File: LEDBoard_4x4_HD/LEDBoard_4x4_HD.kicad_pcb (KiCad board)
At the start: 4 copper layers, 25 x 10 mm, 17 parts, among them U1 TLC5957

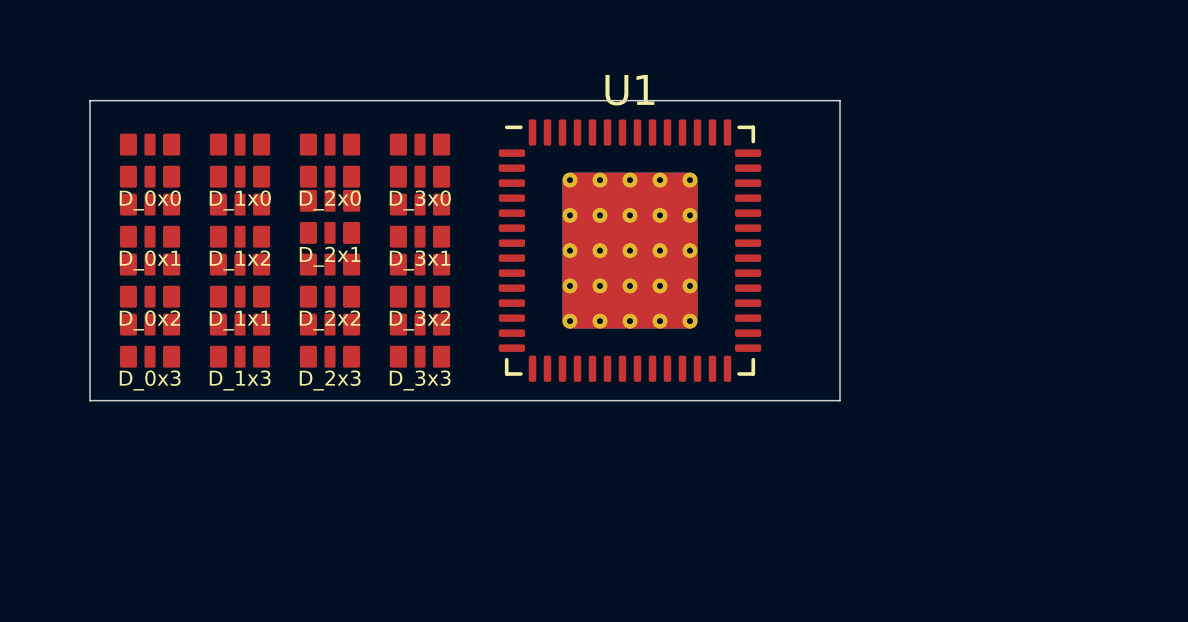
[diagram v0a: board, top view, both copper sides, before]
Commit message: LEDBoard parts positioned & routing started
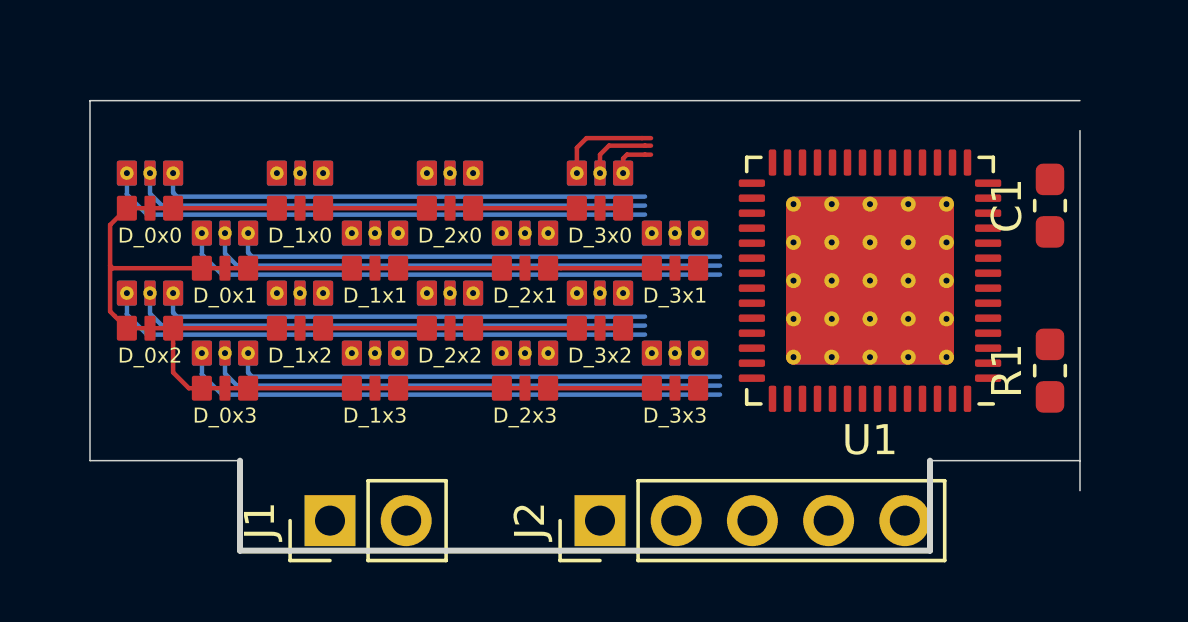
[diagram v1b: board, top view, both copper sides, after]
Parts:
- added C1: 0.1uF, Capacitor_SMD:C_0603_1608Metric_Pad1.05x0.95mm_HandSolder, F.Cu at (132.0, 103.5)
- added J1: power, Connector_PinHeader_2.54mm:PinHeader_1x02_P2.54mm_Vertical, F.Cu at (108.0, 114.0)
- added J2: data, Connector_PinHeader_2.54mm:PinHeader_1x05_P2.54mm_Vertical, F.Cu at (117.0, 114.0)
- added R1: 7.5KOhm 0.1%, Resistor_SMD:R_0603_1608Metric_Pad1.05x0.95mm_HandSolder, F.Cu at (132.0, 109.0)
- D_0x0, D_0x1, D_0x2, D_0x3, D_1x0, D_1x1, D_1x2, D_1x3, D_2x0, D_2x1, D_2x2, D_2x3, D_3x0, D_3x1, D_3x2, D_3x3: footprint LEDs_SMD_NICHIA:LED_RGB_0706_1816Metric_ROHM__VeryNarow -> LEDs_SMD_NICHIA:LED_RGB_0706_1816Metric_ROHM_ThermalVias
- U1: footprint Package_DFN_QFN:QFN-56-1EP_8x8mm_P0.5mm_EP4.5x5.2mm_ThermalVias -> Package_DFN_QFN:QFN-56-1EP_8x8mm_P0.5mm_EP5.6x5.6mm_ThermalVias
- moved D_3x1 8.56 mm to (119.5, 105.0)
- moved D_3x3 8.56 mm to (119.5, 109.0)
- moved U1 8.06 mm to (126.0, 106.0), turned to 180 degrees
- moved D_2x1 6.60 mm to (114.5, 105.0)
- moved D_2x3 6.58 mm to (114.5, 109.0)
- moved D_3x0 6.08 mm to (117.0, 103.0)
- moved D_3x2 6.08 mm to (117.0, 107.0)
- moved D_1x1 4.61 mm to (109.5, 105.0)
- moved D_1x3 4.61 mm to (109.5, 109.0)
- moved D_2x0 4.12 mm to (112.0, 103.0)
- moved D_2x2 4.12 mm to (112.0, 107.0)
- moved D_1x2 3.61 mm to (107.0, 107.0)
- moved D_0x1 2.69 mm to (104.5, 105.0)
- moved D_0x3 2.69 mm to (104.5, 109.0)
- moved D_1x0 2.24 mm to (107.0, 103.0)
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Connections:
- U1 pad 1: (no net) -> /IREF
- U1 pad 10: (no net) -> /led_0x0_b
- U1 pad 11: (no net) -> /led_1x0_r
- U1 pad 12: (no net) -> /led_1x0_g
- U1 pad 13: (no net) -> /led_1x0_b
- U1 pad 14: (no net) -> /led_2x0_r
- U1 pad 15: (no net) -> /led_2x0_g
- U1 pad 16: (no net) -> /led_2x0_b
- U1 pad 17: (no net) -> /led_3x0_r
- U1 pad 18: (no net) -> /led_3x0_g
- U1 pad 19: (no net) -> /led_3x0_b
- U1 pad 2: (no net) -> /led_2x3_r
- U1 pad 20: (no net) -> /led_0x1_r
- U1 pad 21: (no net) -> /led_0x1_g
- U1 pad 22: (no net) -> /led_0x1_b
- U1 pad 23: (no net) -> /led_1x1_r
- U1 pad 24: (no net) -> /led_1x1_g
- U1 pad 25: (no net) -> /led_1x1_b
- U1 pad 26: (no net) -> /SIN
- U1 pad 27: (no net) -> /LAT
- U1 pad 28: (no net) -> /SCLK
- U1 pad 29: (no net) -> /GCLK
- U1 pad 3: (no net) -> /led_2x3_g
- U1 pad 30: (no net) -> /led_2x1_r
- U1 pad 31: (no net) -> /led_2x1_g
- U1 pad 32: (no net) -> /led_2x1_b
- U1 pad 33: (no net) -> /led_3x1_r
- U1 pad 34: (no net) -> /led_3x1_g
- U1 pad 35: (no net) -> /led_3x1_b
- U1 pad 36: (no net) -> /led_0x2_r
- U1 pad 37: (no net) -> /led_0x2_g
- U1 pad 38: (no net) -> /led_0x2_b
- U1 pad 39: (no net) -> /led_1x2_r
- U1 pad 4: (no net) -> /led_2x3_b
- U1 pad 40: (no net) -> /led_1x2_g
- U1 pad 41: (no net) -> /led_1x2_b
- U1 pad 42: (no net) -> /SOUT
- U1 pad 43: (no net) -> VCC
- U1 pad 44: (no net) -> /led_2x2_r
- U1 pad 45: (no net) -> /led_2x2_g
- U1 pad 46: (no net) -> /led_2x2_b
- U1 pad 47: (no net) -> /led_3x2_r
- U1 pad 48: (no net) -> /led_3x2_g
- U1 pad 49: (no net) -> /led_3x2_b
- U1 pad 5: (no net) -> /led_3x3_r
- U1 pad 50: (no net) -> /led_0x3_r
- U1 pad 51: (no net) -> /led_0x3_g
- U1 pad 52: (no net) -> /led_0x3_b
- U1 pad 53: (no net) -> /led_1x3_r
- U1 pad 54: (no net) -> /led_1x3_g
- U1 pad 55: (no net) -> /led_1x3_b
- U1 pad 56: (no net) -> GND
- U1 pad 57: (no net) -> GND
- U1 pad 6: (no net) -> /led_3x3_g
- U1 pad 7: (no net) -> /led_3x3_b
- U1 pad 8: (no net) -> /led_0x0_r
- U1 pad 9: (no net) -> /led_0x0_g
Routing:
- net VCC: track 0.00 -> 76.4 mm
- net /led_0x3_r: track 0.00 -> 18.3 mm
- net /led_0x2_r: track 0.00 -> 18.3 mm
- net /led_0x1_r: track 0.00 -> 18.3 mm
- net /led_0x0_r: track 0.00 -> 18.3 mm
- net /led_0x3_g: track 0.00 -> 17.4 mm
- net /led_0x2_g: track 0.00 -> 17.4 mm
- net /led_0x1_g: track 0.00 -> 17.4 mm
- net /led_0x0_g: track 0.00 -> 17.4 mm
- net /led_0x3_b: track 0.00 -> 16.4 mm
- net /led_0x2_b: track 0.00 -> 16.4 mm
- net /led_0x1_b: track 0.00 -> 16.4 mm
- net /led_0x0_b: track 0.00 -> 16.4 mm
- net /led_1x3_r: track 0.00 -> 13.3 mm
- net /led_1x2_r: track 0.00 -> 13.3 mm
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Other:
- board size 25 x 10 mm -> 33 x 15 mm
- net class Default: clearance 0.1 -> 0.15
- rule trace_clearance: 0.1 -> 0.15

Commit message: first routing done
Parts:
- added C2: 0.1uF, Capacitor_SMD:C_0603_1608Metric_Pad1.05x0.95mm_HandSolder, F.Cu at (132.1, 105.3)
- added C3: 0.1uF, Capacitor_SMD:C_0603_1608Metric_Pad1.05x0.95mm_HandSolder, F.Cu at (102.0, 110.0)
- moved J2 6.44 mm to (110.6, 113.1)
- moved J1 3.32 mm to (104.8, 113.1)
- moved C1 1.70 mm to (132.1, 101.8), turned to 270 degrees
- moved R1 0.81 mm to (132.1, 109.8)
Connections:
- J2 pad 2: /LAT -> /SCLK
- J2 pad 3: /SCLK -> /LAT
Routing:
- net GND: track 0.00 -> 44.0 mm, vias 0 -> 10
- net VCC: track 76.4 -> 101.5 mm, vias 0 -> 3
- net /led_3x3_b: track 0.00 -> 24.0 mm, vias 0 -> 3
- net /GCLK: track 0.00 -> 22.1 mm, vias 0 -> 2
- net /led_3x3_r: track 0.00 -> 21.3 mm, vias 0 -> 3
- net /led_3x3_g: track 0.00 -> 20.0 mm, vias 0 -> 3
- net /SCLK: track 0.00 -> 19.8 mm, vias 0 -> 2
- net /led_0x0_r: track 18.3 -> 38.1 mm, vias 0 -> 1
- net /LAT: track 0.00 -> 18.2 mm, vias 0 -> 2
- net /led_0x0_g: track 17.4 -> 35.3 mm, vias 0 -> 1
- net /SIN: track 0.00 -> 17.8 mm, vias 0 -> 2
- net /led_1x0_r: track 13.3 -> 31.0 mm, vias 0 -> 1
- net /led_0x0_b: track 16.4 -> 33.2 mm, vias 0 -> 1
- net /led_2x0_r: track 8.26 -> 24.8 mm, vias 0 -> 1
- net /led_1x0_g: track 12.4 -> 28.7 mm, vias 0 -> 1
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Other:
- board size 33 x 15 mm -> 33 x 13.6 mm
- net class power added: clearance 0.1, trace_width 0.2, via_dia 0.45, via_drill 0.2
- net class signals added: clearance 0.1, trace_width 0.15, via_dia 0.45, via_drill 0.2

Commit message: first layout finished
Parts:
- moved J1 0.20 mm to (104.6, 113.1)
- moved J2 0.20 mm to (110.8, 113.1)
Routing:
- net /SOUT: track 9.29 -> 7.53 mm
- net /SIN: track 17.8 -> 16.4 mm
- net /led_3x3_b: track 24.0 -> 22.7 mm
- net /led_2x3_b: track 21.9 -> 23.2 mm
- net GND: track 44.0 -> 45.1 mm
- net VCC: track 101.5 -> 100.6 mm
- net /LAT: track 18.2 -> 17.5 mm
- net /led_3x0_r: track 15.4 -> 14.7 mm
- net /led_0x0_r: track 38.1 -> 37.4 mm
- net /led_3x0_b: track 11.6 -> 12.2 mm
- added copper zone on B.Cu, net GND
- added copper zone on In1.Cu, net GND
- added copper zone on In2.Cu, net GND
- added copper zone on F.Cu, net VCC
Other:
- outline, holes or cut-outs redrawn
